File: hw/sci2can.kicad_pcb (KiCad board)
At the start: 2 copper layers, 31.1 x 32 mm, 34 parts, among them IC1 MC9S08DZ60xLC, J1 BDM, J2 Screw Terminal, Q1 4MHz, Q2 MGSF1N03L*, U1 uA7805, U2 PCA82C251

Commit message: hw 1v02
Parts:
- removed C1: 1uF, Capacitor_SMD:C_0603_1608Metric_Pad1.05x0.95mm_HandSolder
- removed C4: 22pF, Capacitor_SMD:C_0603_1608Metric_Pad1.05x0.95mm_HandSolder
- removed D1: LL4007, Diode_SMD:D_SMB
- removed D2: POWER*, Diode_SMD:D_0603_1608Metric_Pad1.05x0.95mm_HandSolder
- removed D3: STATUS, Diode_SMD:D_0603_1608Metric_Pad1.05x0.95mm_HandSolder
- removed D4: STOUT*, Diode_SMD:D_0603_1608Metric_Pad1.05x0.95mm_HandSolder
- removed IC1: MC9S08DZ60xLC, Package_QFP:LQFP-32_7x7mm_P0.8mm
- removed Q2: MGSF1N03L*, Package_TO_SOT_SMD:SOT-23
- removed R1: 680*, Resistor_SMD:R_0603_1608Metric_Pad1.05x0.95mm_HandSolder
- removed R13: 10k*, Resistor_SMD:R_0603_1608Metric_Pad1.05x0.95mm_HandSolder
- removed R14: 5k*, Resistor_SMD:R_0603_1608Metric_Pad1.05x0.95mm_HandSolder
- removed R8: 100, Resistor_SMD:R_0603_1608Metric_Pad1.05x0.95mm_HandSolder
- added Cq1: 22pF, Capacitor_SMD:C_0603_1608Metric_Pad1.05x0.95mm_HandSolder, B.Cu at (213.7, 79.0)
- added Cs1: 10uF 50V, Capacitor_SMD:C_Elec_5x5.8, F.Cu at (222.0, 94.2)
- added Cs2: 1uF, Capacitor_SMD:C_0603_1608Metric_Pad1.05x0.95mm_HandSolder, B.Cu at (218.6, 88.8)
- added Cs3: 220pF, Capacitor_SMD:C_0603_1608Metric_Pad1.05x0.95mm_HandSolder, B.Cu at (221.6, 85.1)
- added Cs6: 10uF, Capacitor_SMD:C_0603_1608Metric_Pad1.05x0.95mm_HandSolder, B.Cu at (217.8, 78.8)
- added Di1: BZT52C4V7, Diode_SMD:D_SOD-123, B.Cu at (217.4, 95.0)
- added Dl1: STATUS, Diode_SMD:D_0603_1608Metric_Pad1.05x0.95mm_HandSolder, B.Cu at (211.1, 89.5)
- added Ds1: LL4007, Diode_SMD:D_SMB, F.Cu at (214.2, 95.0)
- added Ds2: SMAJ33A 38.7V, Diode_SMD:D_SMA, F.Cu at (223.4, 87.7)
- added Ds3: SS34, Diode_SMD:D_SMA, F.Cu at (223.4, 80.0)
- added Ls1: 47uH, Inductor_SMD:L_2816_7142Metric_Pad3.20x4.45mm_HandSolder, F.Cu at (218.7, 80.8)
- added Rc1: 100, Resistor_SMD:R_0603_1608Metric_Pad1.05x0.95mm_HandSolder, B.Cu at (201.4, 95.8)
- added Ri7: 10k, Resistor_SMD:R_0603_1608Metric_Pad1.05x0.95mm_HandSolder, B.Cu at (215.1, 95.7)
- added Ri8: 1k, Resistor_SMD:R_0603_1608Metric_Pad1.05x0.95mm_HandSolder, B.Cu at (214.1, 93.1)
- added Ri9: ?*, Resistor_SMD:R_0603_1608Metric_Pad1.05x0.95mm_HandSolder, B.Cu at (213.1, 95.7)
- added Rs3: 1M, Resistor_SMD:R_0603_1608Metric_Pad1.05x0.95mm_HandSolder, B.Cu at (220.7, 88.8)
- added Rs4: 3k, Resistor_SMD:R_0603_1608Metric_Pad1.05x0.95mm_HandSolder, B.Cu at (217.8, 85.1)
- added Rs5: 10k, Resistor_SMD:R_0603_1608Metric_Pad1.05x0.95mm_HandSolder, B.Cu at (219.7, 85.1)
- added T1: TSM2308*, Package_TO_SOT_SMD:SOT-23, F.Cu at (208.2, 95.5)
- added T2: TSM2308*, Package_TO_SOT_SMD:SOT-23, F.Cu at (204.2, 95.5)
- added uC1: MC9S08DZ60xLC, Package_QFP:LQFP-32_7x7mm_P0.8mm, F.Cu at (209.1, 87.2)
- Cs4: renamed from C2; value 10nF -> 1uF
- Cs5: renamed from C3; value 1uF -> 10uF
- Di2: renamed from D5; value 4V7 -> BZT52C4V7; footprint Diode_SMD:D_1206_3216Metric_Pad1.42x1.75mm_HandSolder -> Diode_SMD:D_SOD-123
- J1: footprint Connector_PinHeader_2.54mm:PinHeader_2x03_P2.54mm_Vertical -> Connector_PinHeader_2.54mm:PinHeader_2x05_P2.54mm_Vertical
- Rb1: renamed from R10; value 10k* -> 10k
- Rc2: renamed from RT1; value 120 -> 100
- Ri4: renamed from R6; value Reserved* -> ?*
- Rl1: renamed from R12; value 680 -> 1k
- Rs1: renamed from R2; value 100k* -> 100k
- Rs2: renamed from R3; value 10k* -> 10k
- U1: value uA7805 -> ME3116; footprint Package_TO_SOT_THT:TO-220-3_Horizontal_TabDown -> Package_TO_SOT_SMD:SOT-23-6_Handsoldering
- moved Cs5 70.7 mm to (219.6, 78.8), turned to 90 degrees
- moved Ri3 64.4 mm to (207.5, 93.1)
- moved Di2 64.0 mm to (204.2, 95.0), turned to 270 degrees
- moved U1 63.7 mm to (219.7, 88.8), turned to 90 degrees
- moved Ri2 61.0 mm to (208.6, 95.7), turned to 270 degrees
- moved Rc2 60.7 mm to (198.8, 95.8), turned to 270 degrees
- moved Ri1 60.7 mm to (210.6, 95.7), turned to 270 degrees
- moved Ci2 59.5 mm to (206.6, 95.7), turned to 270 degrees
- moved Rr1 58.4 mm to (203.7, 81.8), turned to 0 degrees
- moved Rs1 58.4 mm to (215.6, 85.1), turned to 90 degrees
- moved Cs4 58.4 mm to (211.1, 85.1)
- moved Rb1 58.4 mm to (206.8, 85.1)
- moved Ri4 58.4 mm to (208.9, 85.1)
- moved Rl1 57.8 mm to (213.3, 85.1), turned to 270 degrees
- moved Cq2 57.3 mm to (204.7, 79.0), turned to 90 degrees
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- renumbered C7 to Ci2, C5 to Cq2, C6 to Cr1, R7 to Ri1, R4 to Ri2, R5 to Ri3, R9 to Rq1, R11 to Rr1
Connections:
- Ci2 pad 1: Net-(C7-Pad1) -> Net-(Ci2-Pad1)
- Ci2 pad 2: IN -> IO2
- Cs4 pad 1: +5V -> +3V3
- Cs5 pad 1: +5V -> +3V3
- Di2 pad 1: RxD1 -> Net-(Ci2-Pad1)
- J1 pad 3: RXCAN -> TxD1
- J1 pad 5: TXCAN -> RxD1
- J1 pad 6: +5V -> +3V3
- J2 pad 3: OUT -> IO2
- J2 pad 4: IN -> IO1
- Rb1 pad 1: +5V -> +3V3
- Ri1 pad 1: IN -> IO2
- Ri2 pad 1: Net-(C7-Pad1) -> Net-(Ci2-Pad1)
- Ri2 pad 2: IN -> IO2
- Ri3 pad 2: Net-(C7-Pad1) -> Net-(Ci2-Pad1)
- Rr1 pad 1: +5V -> RESET
- Rr1 pad 2: RESET -> +3V3
- U1 pad 3: +5V -> Net-(Cs3-Pad1)
- U2 pad 3: +5V -> +3V3
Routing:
- net +3V3: track 0.00 -> 53.0 mm, vias 0 -> 3
- net +5V: track 47.3 -> 0.00 mm, vias 1 -> 0
- net Net-(Cs1-Pad1): track 0.00 -> 20.7 mm, vias 0 -> 1
- net IO2: track 0.00 -> 19.3 mm
- net IO1: track 0.00 -> 15.7 mm
- net GND: track 8.17 -> 23.0 mm, vias 3 -> 31
- net UZ: track 39.3 -> 24.4 mm, vias 2 -> 1
- net OUT: track 13.1 -> 0.00 mm
- net FET: track 12.8 -> 0.00 mm, vias 1 -> 0
- net TxD1: track 0.00 -> 10.8 mm
- net Net-(Cs3-Pad1): track 0.00 -> 10.4 mm, vias 0 -> 1
- net Net-(Cs2-Pad2): track 0.00 -> 9.32 mm, vias 0 -> 1
- net SDA: track 0.00 -> 8.73 mm
- net CANL: track 15.8 -> 7.24 mm, vias 0 -> 1
- net PTE3: track 0.00 -> 8.25 mm
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- added copper zone on F.Cu, net GND
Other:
- board size 31.1 x 32 mm -> 30 x 29.8 mm
- board text added: "IO1"
- board text added: "IO2"
- board text added: "JLCJLCJLCJLC"
- board text added: "github/ butyi/ sci2can V1.02"
- board text added: "sci2can V1.02"
- board text removed: "1"
- board text removed: "IN"
- board text removed: "OUT"
- board text removed: "sci2can V1.01 2020.05.17 www.butyi.hu github.com/butyi/sci2can"

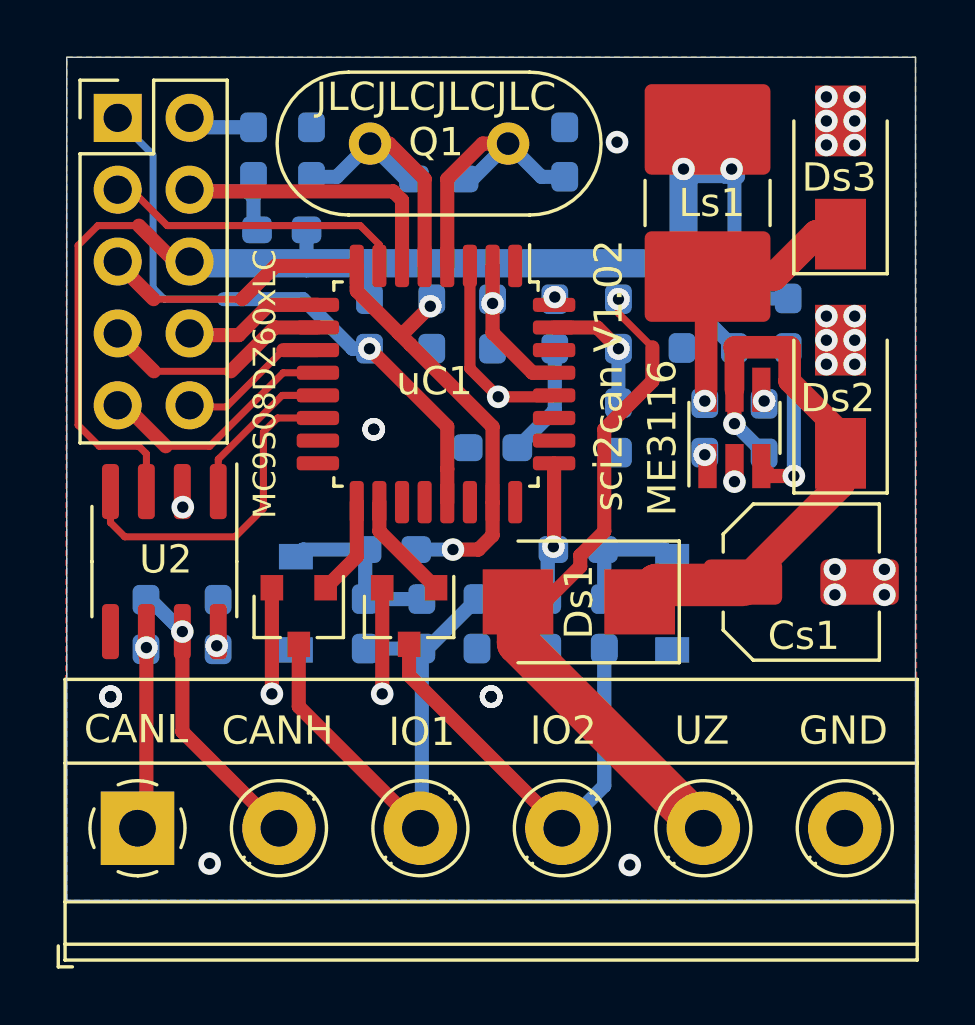
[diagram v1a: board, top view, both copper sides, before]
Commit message: HW SW update, 0.96 inch display
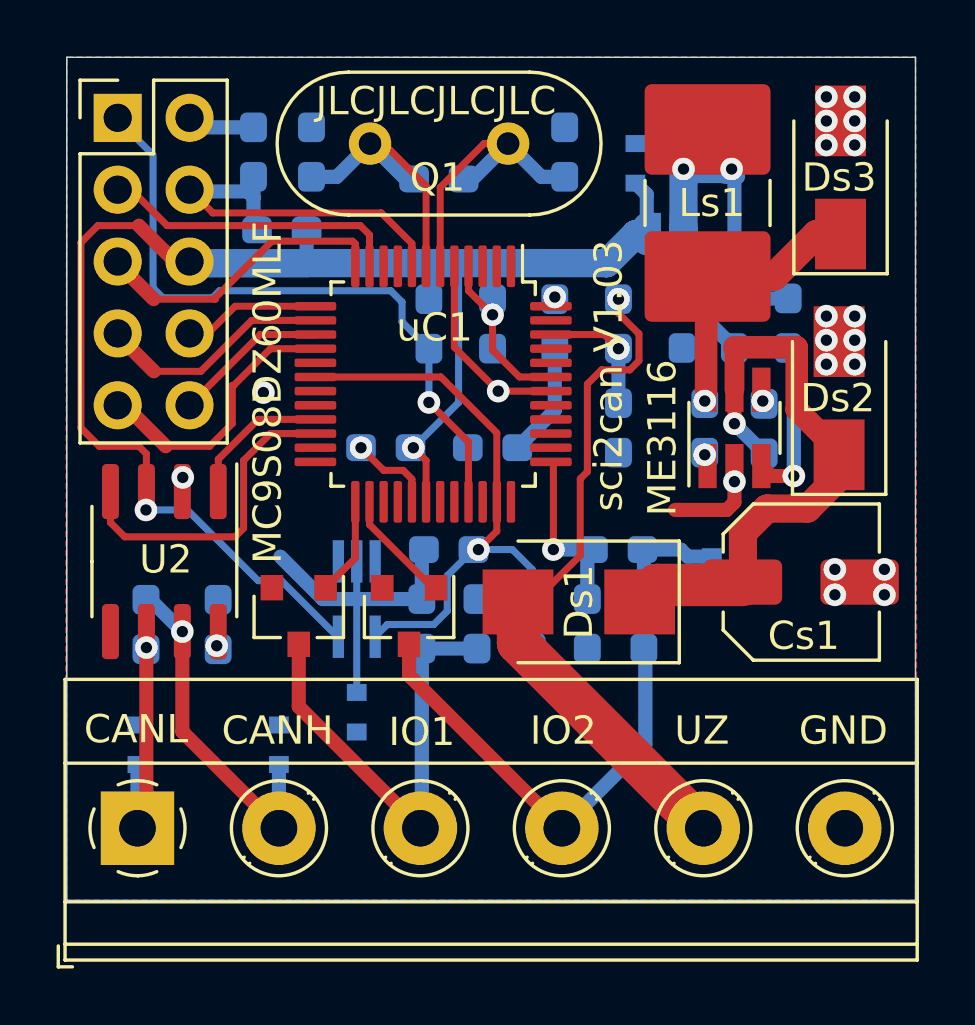
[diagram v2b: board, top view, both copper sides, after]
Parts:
- removed Ci2: 10nF, Capacitor_SMD:C_0603_1608Metric_Pad1.05x0.95mm_HandSolder
- added Cs7: 1uF, Capacitor_SMD:C_0603_1608Metric_Pad1.05x0.95mm_HandSolder, B.Cu at (207.3, 89.5)
- added Dc1: ESD5Z5V0, Diode_SMD:D_SOD-523, B.Cu at (198.6, 100.0)
- added Dc2: ESD5Z5V0, Diode_SMD:D_SOD-523, B.Cu at (203.6, 100.0)
- added Ds4: ESD5Z5V0, Diode_SMD:D_SOD-523, B.Cu at (216.2, 79.5)
- added Js1: Jumper, Jumper:SolderJumper-2_P1.3mm_Open_RoundedPad1.0x1.5mm, B.Cu at (217.2, 82.0)
- added Ui1: 74HC1G125GW, Package_TO_SOT_SMD:SOT-353_SC-70-5_Handsoldering, B.Cu at (206.3, 94.8)
- Cs6: value 10uF -> 100nF
- Di1, Di2: value BZT52C4V7 -> ESD5Z5V0; footprint Diode_SMD:D_SOD-123 -> Diode_SMD:D_SOD-523
- Ds2: value SMAJ33A 38.7V -> SMAJ33A
- Ls1: value 47uH -> 10uH
- Ri3: value 1k -> 1k*
- Rs4: value 3k -> 2k
- uC1: value MC9S08DZ60xLC -> MC9S08DZ60MLF; footprint Package_QFP:LQFP-32_7x7mm_P0.8mm -> Package_QFP:LQFP-48_7x7mm_P0.5mm
- moved Ri4 11.2 mm to (212.5, 95.7)
- moved Di2 4.41 mm to (206.3, 98.8)
- moved Rb1 2.10 mm to (208.8, 85.1)
- moved Ri3 2.03 mm to (209.6, 93.1)
- moved Di1 1.69 mm to (218.8, 94.0)
- moved Ri8 1.40 mm to (215.5, 93.1)
- moved Ri7 1.40 mm to (216.4, 95.7)
- moved Ri9 1.40 mm to (214.4, 95.7)
- moved uC1 0.10 mm to (209.0, 87.2)
- moved Ds2 0.07 mm to (223.3, 87.8)
- turned Ri1 to 90 degrees
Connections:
- Cs3 pad 2: +3V3 -> Net-(Cs3-Pad2)
- Cs4 pad 1: +3V3 -> +5V
- Cs5 pad 1: +3V3 -> Net-(Cs3-Pad2)
- Cs6 pad 1: +3V3 -> Net-(Cs3-Pad2)
- J1 pad 6: +3V3 -> +5V
- Ls1 pad 2: +3V3 -> Net-(Cs3-Pad2)
- Rb1 pad 1: +3V3 -> +5V
- Ri3 pad 1: RxD1 -> RxD2
- Ri4 pad 2: RxD1 -> RxD2
- Rr1 pad 2: +3V3 -> +5V
- Rs5 pad 1: +3V3 -> Net-(Cs3-Pad2)
- U2 pad 3: +3V3 -> +5V
- uC1 pad 10: PTE3 -> Net-(uC1-Pad10)
- uC1 pad 11: SCL -> TxD1
- uC1 pad 12: SDA -> RxD1
- uC1 pad 13: TXCAN -> PTE2
- uC1 pad 14: RXCAN -> PTE3
- uC1 pad 15: Net-(uC1-Pad15) -> SCL
- uC1 pad 16: Net-(uC1-Pad16) -> SDA
- uC1 pad 17: FET2 -> Net-(uC1-Pad17)
- uC1 pad 18: FET1 -> RxD2
- uC1 pad 2: +3V3 -> Net-(uC1-Pad2)
- uC1 pad 21: BKGD -> TXCAN
- uC1 pad 22: Net-(uC1-Pad22) -> RXCAN
- uC1 pad 23: RxD1 -> Net-(uC1-Pad23)
- uC1 pad 25: IN2 -> FET2
- uC1 pad 26: Net-(uC1-Pad26) -> FET1
- uC1 pad 28: GND -> Net-(uC1-Pad28)
- uC1 pad 29: +3V3 -> GND
- uC1 pad 3: GND -> Net-(uC1-Pad3)
- uC1 pad 30: Net-(uC1-Pad30) -> +5V
- uC1 pad 31: UZ_MEAS -> Net-(uC1-Pad31)
- uC1 pad 32: LED2 -> Net-(uC1-Pad32)
- uC1 pad 4: EXTAL -> +5V
- uC1 pad 5: XTAL -> GND
- uC1 pad 6: RESET -> EXTAL
- uC1 pad 7: TxD1 -> XTAL
- uC1 pad 8: RxD1 -> RESET
- uC1 pad 9: PTE2 -> Net-(uC1-Pad9)
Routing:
- net +5V: track 0.00 -> 62.6 mm, vias 0 -> 3
- net +3V3: track 53.0 -> 0.00 mm, vias 3 -> 0
- net RxD2: track 0.00 -> 20.7 mm, vias 0 -> 1
- net RxD1: track 25.7 -> 10.7 mm, vias 2 -> 0
- net Net-(Cs3-Pad2): track 0.00 -> 10.5 mm, vias 0 -> 2
- net Net-(Di2-Pad1): track 6.37 -> 12.0 mm
- net IO2: track 19.3 -> 16.6 mm
- net CANH: track 10.1 -> 12.4 mm
- net CANL: track 7.24 -> 9.49 mm
- net BKGD: track 21.5 -> 23.6 mm
- net IN2: track 4.86 -> 6.38 mm
- net GND: track 23.0 -> 21.9 mm, vias 31 -> 21
- net SDA: track 8.73 -> 9.78 mm
- net Net-(Cs1-Pad1): track 20.7 -> 21.7 mm
- net IO1: track 15.7 -> 16.3 mm
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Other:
- board text added: "H"
- board text added: "L"
- board text added: "V1.03 github.com/butyi/sci2can"
- board text added: "sci2can V1.03"
- board text removed: "github/ butyi/ sci2can V1.02"
- board text removed: "sci2can V1.02"
